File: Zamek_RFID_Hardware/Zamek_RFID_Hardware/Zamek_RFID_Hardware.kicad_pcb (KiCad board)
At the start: 2 copper layers, 72 x 57.2 mm, 30 parts, among them J1 Conn_01x08, J2 Conn_01x08, J3 Conn_01x04, J4 Conn_01x03, Q1 BC547

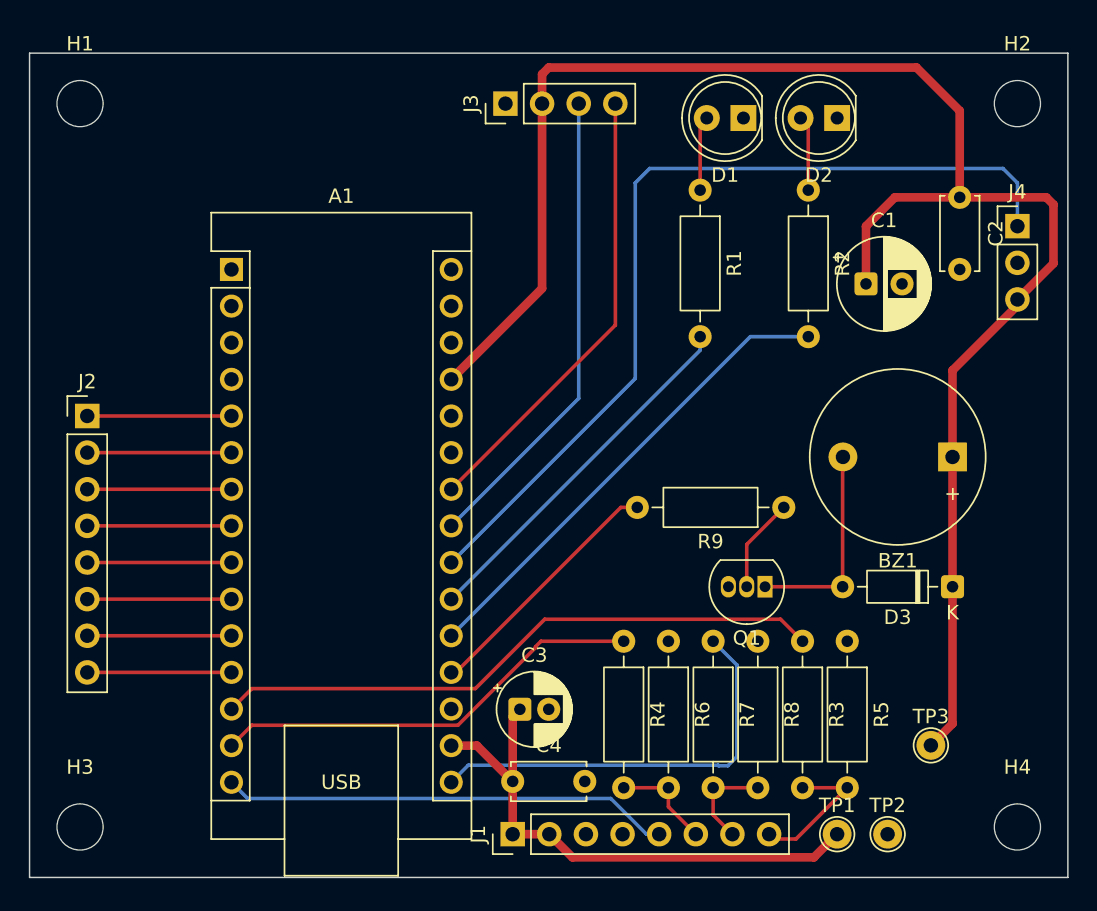
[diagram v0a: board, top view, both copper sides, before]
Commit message: hw: add GND pours on both layers
- thermal reliefs, islands removed
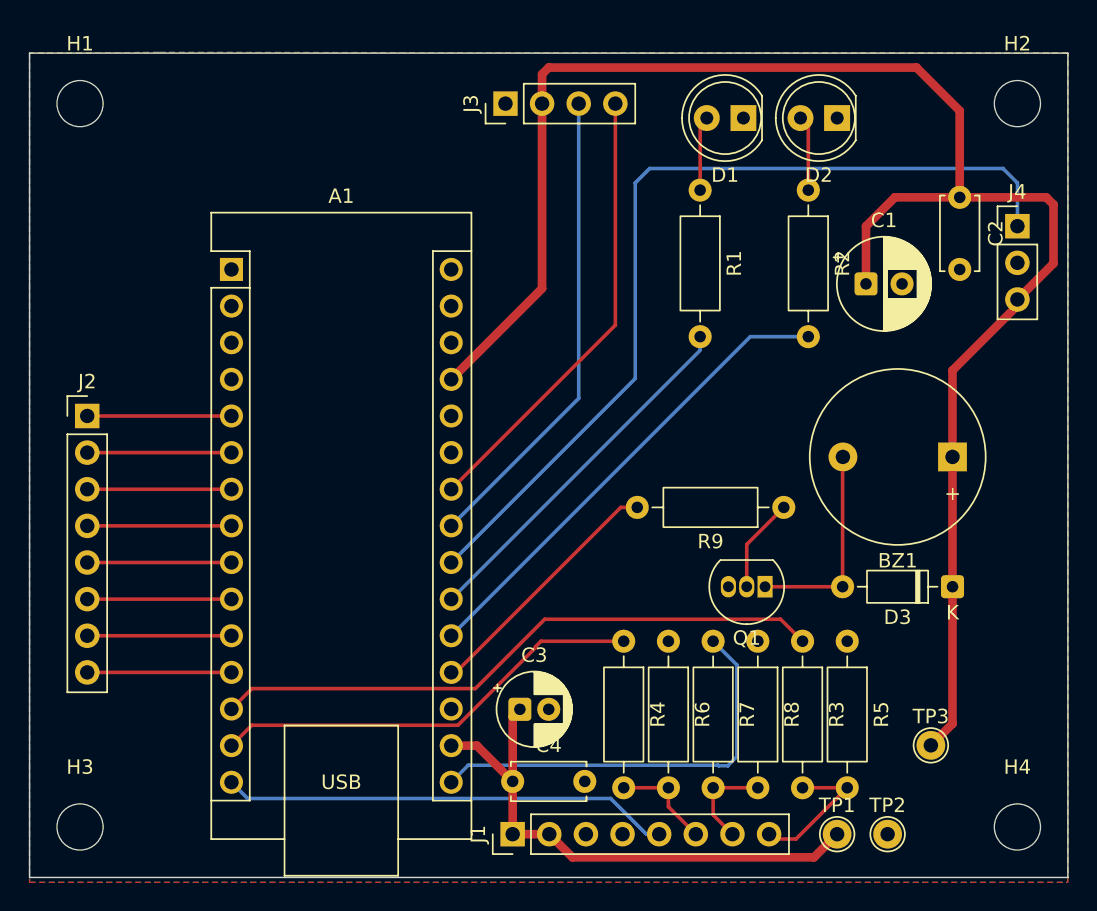
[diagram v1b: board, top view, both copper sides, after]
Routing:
- added copper zone on B.Cu, net GND
- added copper zone on F.Cu, net GND
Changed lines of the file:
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@@
 		(net "/LED_ZIELONA")
+	)
+	(zone
+		(net "GND")
+		(layer "F.Cu")
+		(hatch edge 0.5)
+		(connect_pads
+			(clearance 0.3)
+		)
+		(min_thickness 0.25)
+		(fill yes
+			(thermal_gap 0.5)
+			(thermal_bridge_width 0.5)
+			(island_removal_mode 0)
+		)
+		(polygon
+			(pts
+				(xy 118.967495 68.952409) (xy 110 69) (xy 110 126.5) (xy 182 126.5) (xy 182 69)
+			)
+		)
+	)
+	(zone
+		(net "GND")
+		(layer "B.Cu")
+		(hatch edge 0.5)
+		(connect_pads
+			(clearance 0.3)
+		)
+		(min_thickness 0.25)
+		(fill yes
+			(thermal_gap 0.5)
+			(thermal_bridge_width 0.5)
+			(island_removal_mode 0)
+		)
+		(polygon
+			(pts
+				(xy 118.967495 68.952409) (xy 110 69) (xy 110 126.5) (xy 182 126.5) (xy 182 69)
+			)
+		)
 	)
 	(embedded_fonts no)

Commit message: hw: add silkscreen
- board name, version, connector and pin labels
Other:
- board text added: "2026.09"
- board text added: "3V3"
- board text added: "5V"
- board text added: "C1"
- board text added: "C2"
- board text added: "C3"
- board text added: "C4"
- board text added: "GND"
- board text added: "IN"
- board text added: "IRQ"
- board text added: "KEYPAD"
- board text added: "LCD I2C"
- board text added: "MISO"
- board text added: "MOSI"
- board text added: "R1"
- board text added: "R2"
- board text added: "R3"
- board text added: "R4"
- board text added: "RELAY"
- board text added: "RFID"
- board text added: "RST"
- board text added: "SCK"
- board text added: "SCL"
- board text added: "SDA"
- board text added: "SMART ACCESS v1.1"
- board text added: "TP1:3V3"
- board text added: "TP2:GND"
- board text added: "TP3:5V"

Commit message: hw: fix R6 value notation (2K - 2k)
- consistent with R5/R8, so BOM groups all 2k resistors in one line
- lowercase k is the SI prefix
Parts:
- R6: value 2K -> 2k
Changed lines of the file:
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@@
 			)
 		)
-		(property "Value" "2K"
+		(property "Value" "2k"
 			(at 5.08 2.37 270)
 			(layer "F.Fab")
